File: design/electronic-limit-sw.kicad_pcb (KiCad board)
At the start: 2 copper layers, 98 x 36.2 mm, 35 parts, among them J1 3.5mm - 2-pin screw terminal, J2 3.5mm - 2-pin screw terminal, J3 SMD - 2.54mm 4-pin pad termin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, J4 7.62mm - 4-pin screw terminal, Q1 MMBT2222, U1 PIC10F200-IOT

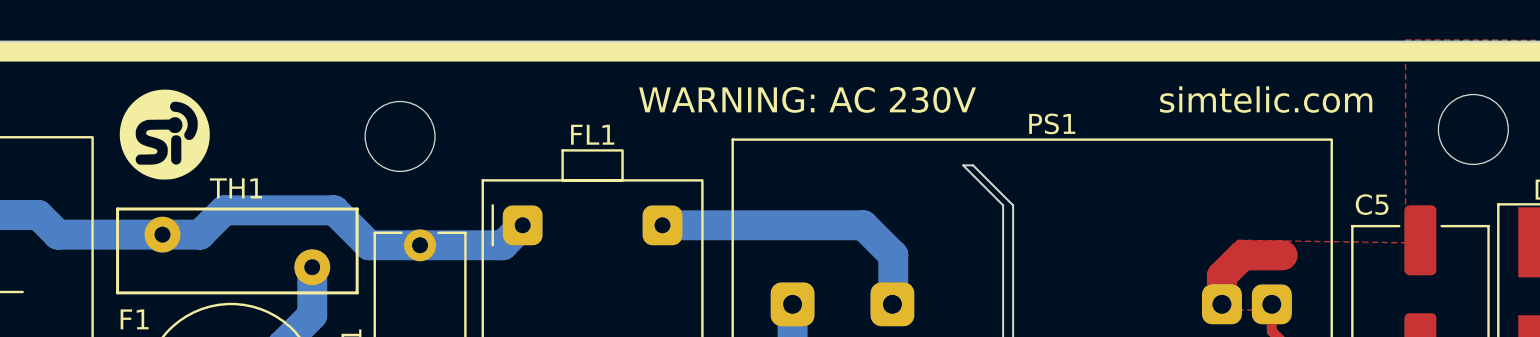
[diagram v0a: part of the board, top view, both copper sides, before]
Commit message: Upgrade project to new KiCAD version.
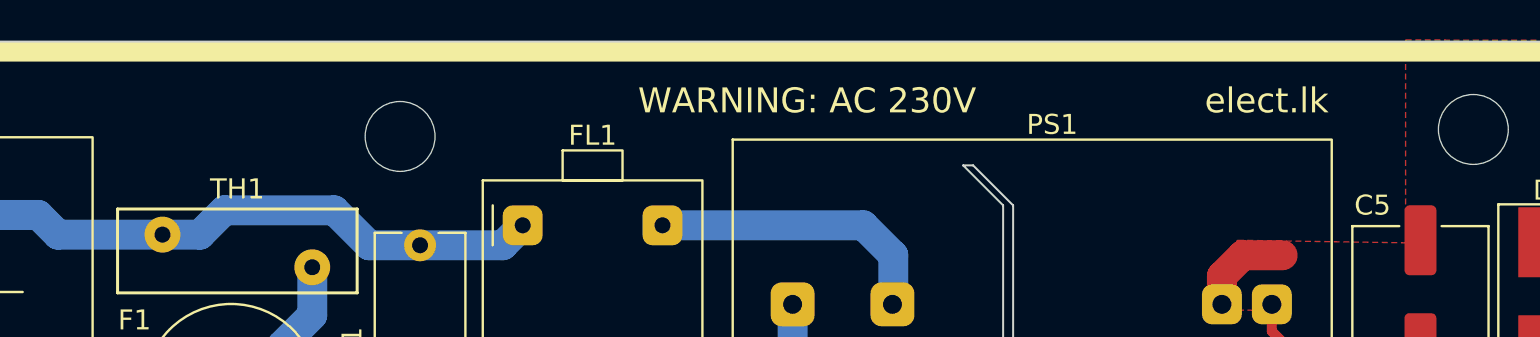
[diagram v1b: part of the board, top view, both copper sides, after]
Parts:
- removed LG1: LOGO, simtelic:simtelic-name-5
- removed LG2: LOGO, simtelic:simtelic-5
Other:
- board text added: "elect.lk"
- board text removed: "EL0006"
- board text removed: "M"
- board text removed: "REV 1.0.0"
- board text removed: "simtelic.com"
